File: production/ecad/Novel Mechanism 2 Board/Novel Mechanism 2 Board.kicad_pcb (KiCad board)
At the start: 2 copper layers, 41.7 x 46.1 mm, 19 parts, among them J1 1755736, J2 1755736, J3 0532611271, U1 L9958SBTR, U2 TMCS1108A4BQDRQ1

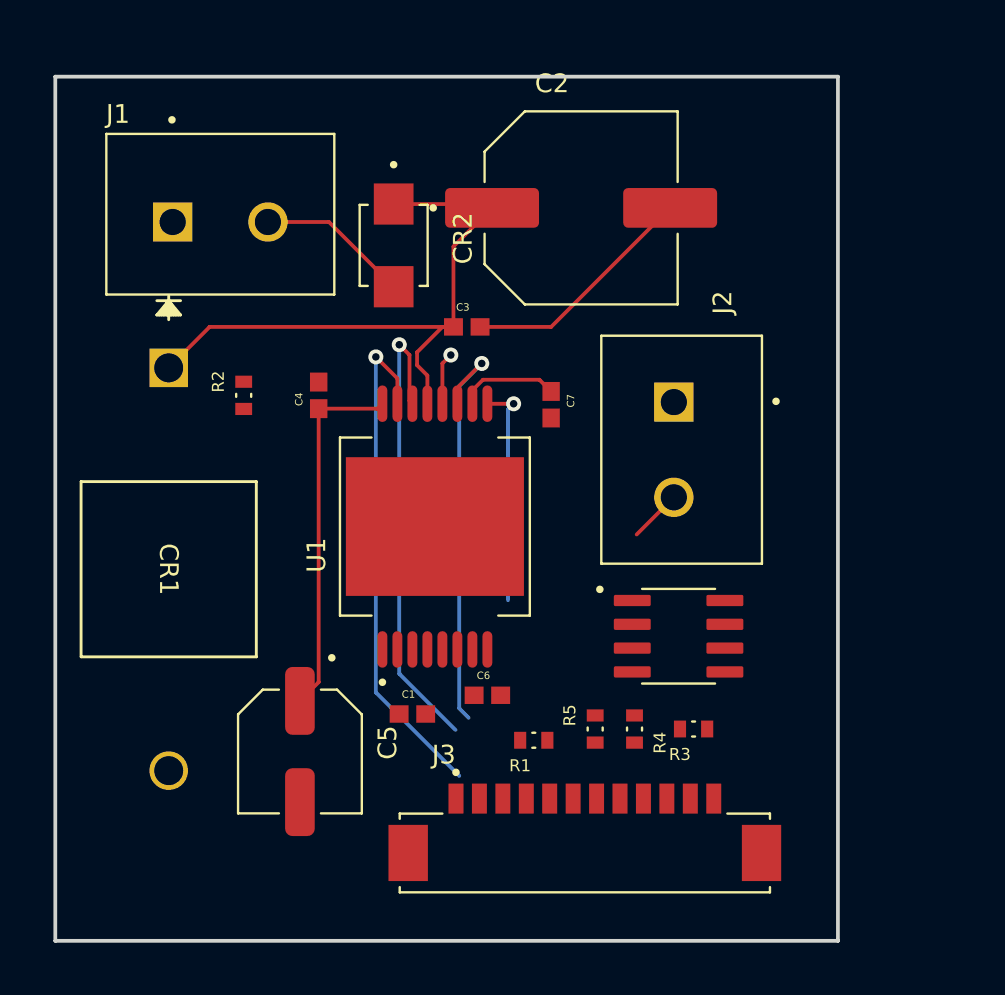
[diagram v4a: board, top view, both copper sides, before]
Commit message: updated design constraints
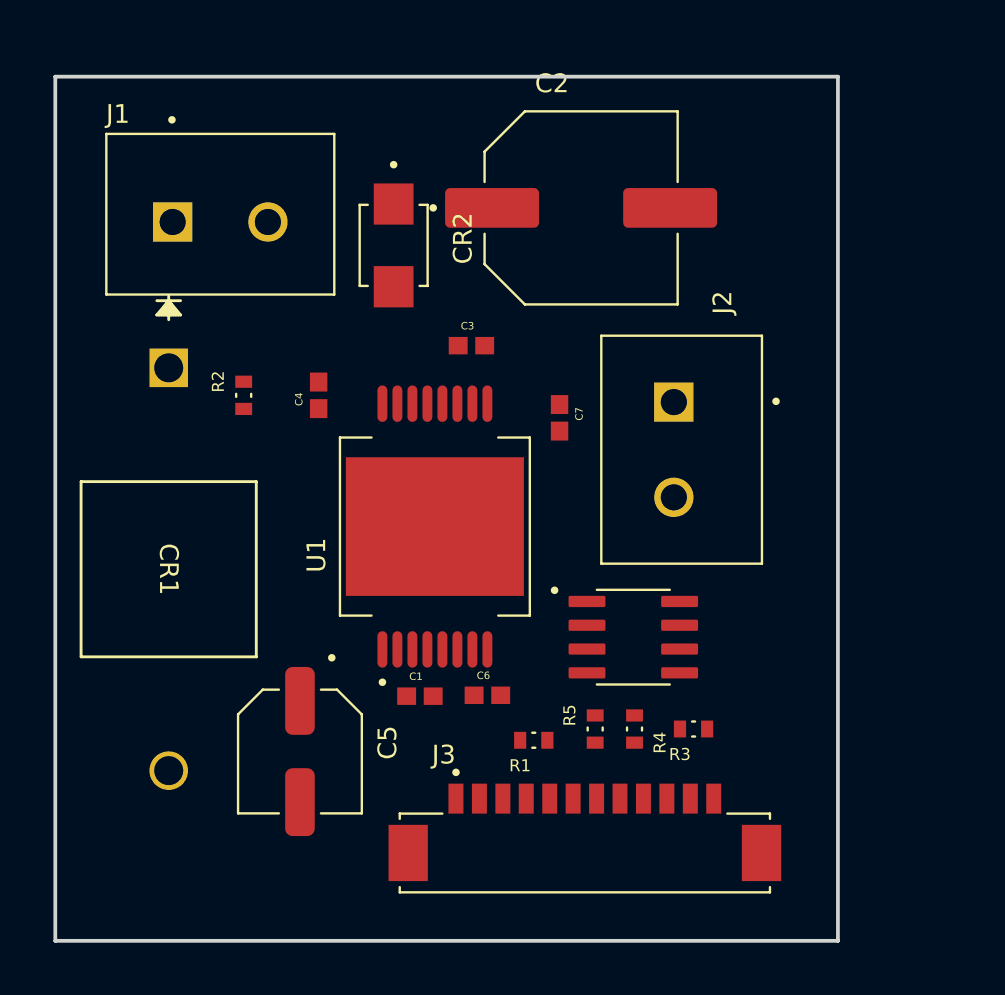
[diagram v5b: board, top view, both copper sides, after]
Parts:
- moved U2 2.42 mm to (147.8, 75.9)
- moved C1 1.03 mm to (136.4, 79.0)
- moved C3 1.03 mm to (139.2, 60.4)
- moved C7 0.83 mm to (143.8, 64.2)
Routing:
- net +15V: track 34.1 -> 0.00 mm
- net /SCK: track 27.2 -> 0.00 mm, vias 1 -> 0
- net /SI: track 25.2 -> 0.00 mm, vias 1 -> 0
- net /PWM: track 22.3 -> 0.00 mm, vias 1 -> 0
- net +5V: track 19.7 -> 0.00 mm
- net GND: track 12.8 -> 0.00 mm
- net /Enable: track 12.7 -> 0.00 mm, vias 1 -> 0
- net Net-(CR2-Pad2): track 8.14 -> 0.00 mm
- net Net-(U1-OUT2): track 5.40 -> 0.00 mm
- net Net-(U2-IN-): track 2.80 -> 0.00 mm
- net Net-(U1-REXT): track 2.78 -> 0.00 mm, vias 1 -> 0
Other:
- copper layers 2 -> 4
- rule pad_to_mask_clearance: 0.05 -> 0
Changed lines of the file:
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@@
   (layers
     (0 "F.Cu" signal)
+    (1 "In1.Cu" power)
+    (2 "In2.Cu" power)
     (31 "B.Cu" signal)
     (32 "B.Adhes" user "B.Adhesive")
@@
       (layer "F.Mask" (type "Top Solder Mask") (thickness 0.01))
       (layer "F.Cu" (type "copper") (thickness 0.035))
-      (layer "dielectric 1" (type "core") (thickness 1.51) (material "FR4") (epsilon_r 4.5) (loss_tangent 0.02))
+      (layer "dielectric 1" (type "prepreg") (thickness 0.1) (material "FR4") (epsilon_r 4.5) (loss_tangent 0.02))
+      (layer "In1.Cu" (type "copper") (thickness 0.035))
+      (layer "dielectric 2" (type "core") (thickness 1.24) (material "FR4") (epsilon_r 4.5) (loss_tangent 0.02))
+      (layer "In2.Cu" (type "copper") (thickness 0.035))
+      (layer "dielectric 3" (type "prepreg") (thickness 0.1) (material "FR4") (epsilon_r 4.5) (loss_tangent 0.02))
       (layer "B.Cu" (type "copper") (thickness 0.035))
       (layer "B.Mask" (type "Bottom Solder Mask") (thickness 0.01))
@@
       (dielectric_constraints no)
     )
-    (pad_to_mask_clearance 0.05)
+    (pad_to_mask_clearance 0)
     (solder_mask_min_width 0.1)
     (pcbplotparams
@@
   )
   (footprint "Package_SO:TMCS1108A4BQDRQ1" (layer "F.Cu")
-    (at 150.2 75.85)
+    (at 147.785 75.9)
     (property "A1_MIN" "0.11")
     (property "A_MAX" "1.75")
@@
   )
   (footprint "Capacitor_SMD:CAP_0603" (layer "F.Cu")
-    (at 138.9 59.35)
+    (at 139.15 60.35)
     (property "Sheetfile" "Novel Mechanism 2 Board.kicad_sch")
     (property "Sheetname" "")
@@
   )
   (footprint "Capacitor_SMD:CAP_0603" (layer "F.Cu")
-    (at 143.4 63.5 -90)
+    (at 143.85 64.2 -90)
     (property "Sheetfile" "Novel Mechanism 2 Board.kicad_sch")
     (property "Sheetname" "")
@@
   )
   (footprint "Capacitor_SMD:CAP_0603" (layer "F.Cu")
-    (at 136 80)
+    (at 136.4 79.05)
     (property "Sheetfile" "Novel Mechanism 2 Board.kicad_sch")
     (property "Sheetname" "")
@@
   (gr_rect (start 116.95 46) (end 158.7 92.1)
     (stroke (width 0.2) (type default)) (fill none) (layer "Edge.Cuts"))
-  (segment (start 136.8 63.445) (end 136.8 61.942213) (width 0.2032) (layer "F.Cu") (net 1))
-  (segment (start 138.191 59.35) (end 138.191 55.059) (width 0.2032) (layer "F.Cu") (net 1))
-  (segment (start 138.191 55.059) (end 140.25 53) (width 0.2032) (layer "F.Cu") (net 1))
-  (segment (start 138.191 59.35) (end 125.18215 59.35) (width 0.2032) (layer "F.Cu") (net 1))
-  (segment (start 136.2484 61.390613) (end 136.2484 60.7016) (width 0.2032) (layer "F.Cu") (net 1))
-  (segment (start 137.6 59.35) (end 138.191 59.35) (width 0.2032) (layer "F.Cu") (net 1))
-  (segment (start 136.8 61.942213) (end 136.2484 61.390613) (width 0.2032) (layer "F.Cu") (net 1))
-  (segment (start 136.2484 60.7016) (end 137.6 59.35) (width 0.2032) (layer "F.Cu") (net 1))
-  (segment (start 125.18215 59.35) (end 123 61.53215) (width 0.2032) (layer "F.Cu") (net 1))
-  (segment (start 140.045 52.795) (end 140.25 53) (width 0.2032) (layer "F.Cu") (net 1))
-  (segment (start 135 52.795) (end 140.045 52.795) (width 0.2032) (layer "F.Cu") (net 1))
-  (segment (start 134.291 63.336) (end 134.4 63.445) (width 0.2032) (layer "F.Cu") (net 4))
-  (segment (start 134.136 63.709) (end 131 63.709) (width 0.2032) (layer "F.Cu") (net 4))
-  (segment (start 131 78.3) (end 130 79.3) (width 0.2032) (layer "F.Cu") (net 4))
-  (segment (start 131 63.709) (end 131 78.3) (width 0.2032) (layer "F.Cu") (net 4))
-  (segment (start 134.4 63.445) (end 134.136 63.709) (width 0.2032) (layer "F.Cu") (net 4))
-  (segment (start 143.4 59.35) (end 149.75 53) (width 0.2032) (layer "F.Cu") (net 5))
-  (segment (start 139.609 59.35) (end 143.4 59.35) (width 0.2032) (layer "F.Cu") (net 5))
-  (segment (start 142.7774 62.1684) (end 139.765307 62.1684) (width 0.2032) (layer "F.Cu") (net 7))
-  (segment (start 139.2 62.733707) (end 139.2 63.445) (width 0.2032) (layer "F.Cu") (net 7))
-  (segment (start 143.4 62.791) (end 142.7774 62.1684) (width 0.2032) (layer "F.Cu") (net 7))
-  (segment (start 139.765307 62.1684) (end 139.2 62.733707) (width 0.2032) (layer "F.Cu") (net 7))
-  (segment (start 128.2925 53.7525) (end 131.5475 53.7525) (width 0.2032) (layer "F.Cu") (net 8))
-  (segment (start 131.5475 53.7525) (end 135 57.205) (width 0.2032) (layer "F.Cu") (net 8))
-  (segment (start 140.005 63.45) (end 140 63.445) (width 0.2032) (layer "F.Cu") (net 9))
-  (segment (start 141.4 63.45) (end 140.005 63.45) (width 0.2032) (layer "F.Cu") (net 9))
-  (segment (start 140 63.445) (end 140 64.156293) (width 0.2032) (layer "F.Cu") (net 9))
-  (via (at 141.4 63.45) (size 0.8) (drill 0.4) (layers "F.Cu" "B.Cu") (net 9))
-  (segment (start 141.4 63.45) (end 141.1 63.75) (width 0.2032) (layer "B.Cu") (net 9))
-  (segment (start 141.1 63.75) (end 141.1 73.925) (width 0.2032) (layer "B.Cu") (net 9))
-  (segment (start 137.6 61.3) (end 137.6 63.445) (width 0.2032) (layer "F.Cu") (net 10))
-  (segment (start 138.05 60.85) (end 137.6 61.3) (width 0.2032) (layer "F.Cu") (net 10))
-  (via (at 138.05 60.85) (size 0.8) (drill 0.4) (layers "F.Cu" "B.Cu") (net 10))
-  (segment (start 139.7 61.3) (end 138.4 62.6) (width 0.2032) (layer "F.Cu") (net 15))
-  (segment (start 138.4 62.6) (end 138.4 63.445) (width 0.2032) (layer "F.Cu") (net 15))
-  (via (at 139.7 61.3) (size 0.8) (drill 0.4) (layers "F.Cu" "B.Cu") (net 15))
-  (segment (start 139.7 61.3) (end 138.5 62.5) (width 0.2032) (layer "B.Cu") (net 15))
-  (segment (start 138.5 62.5) (end 138.5 79.7) (width 0.2032) (layer "B.Cu") (net 15))
-  (segment (start 138.5 79.7) (end 139 80.2) (width 0.2032) (layer "B.Cu") (net 15))
-  (segment (start 135.8452 60.8452) (end 135.3 60.3) (width 0.2032) (layer "F.Cu") (net 16))
-  (segment (start 135.8452 63.2902) (end 135.8452 60.8452) (width 0.2032) (layer "F.Cu") (net 16))
-  (segment (start 136 63.445) (end 135.8452 63.2902) (width 0.2032) (layer "F.Cu") (net 16))
-  (via (at 135.3 60.3) (size 0.8) (drill 0.4) (layers "F.Cu" "B.Cu") (net 16))
-  (segment (start 135.3 77.85) (end 138.3 80.85) (width 0.2032) (layer "B.Cu") (net 16))
-  (segment (start 135.3 60.3) (end 135.3 77.85) (width 0.2032) (layer "B.Cu") (net 16))
-  (segment (start 135.2 63.445) (end 135.2 62.1) (width 0.2032) (layer "F.Cu") (net 17))
-  (segment (start 135.2 62.1) (end 134.05 60.95) (width 0.2032) (layer "F.Cu") (net 17))
-  (via (at 134.05 60.95) (size 0.8) (drill 0.4) (layers "F.Cu" "B.Cu") (net 17))
-  (segment (start 134.05 78.85) (end 138.5 83.3) (width 0.2032) (layer "B.Cu") (net 17))
-  (segment (start 134.05 60.95) (end 134.05 78.85) (width 0.2032) (layer "B.Cu") (net 17))
-  (segment (start 149.9475 68.44) (end 147.965 70.4225) (width 0.2032) (layer "F.Cu") (net 18))
 )

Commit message: signal routing complete!
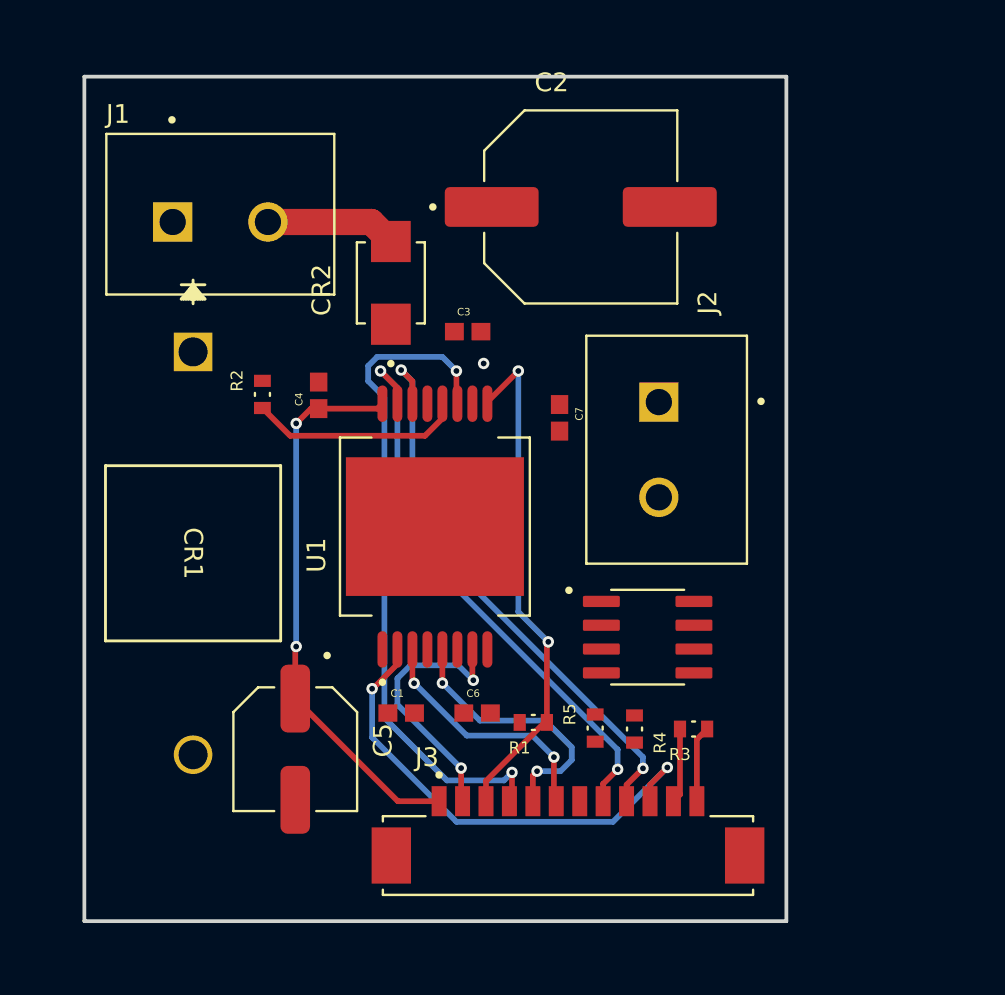
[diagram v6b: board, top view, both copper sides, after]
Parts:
- moved CR2 2.01 mm to (134.8, 57.0), turned to 90 degrees
- moved CR1 1.55 mm to (124.3, 60.7)
- moved C1 1.35 mm to (135.4, 80.0)
- moved C6 1.10 mm to (139.4, 80.0)
- moved R2 1.00 mm to (128.0, 63.0)
- moved R1 0.95 mm to (142.4, 80.5)
- moved J3 0.91 mm to (144.3, 87.5)
- moved J2 0.80 mm to (145.3, 59.8)
- moved C3 0.78 mm to (138.9, 59.6)
- moved U2 0.77 mm to (148.6, 75.9)
- moved C5 0.28 mm to (129.8, 81.9)
- moved C2 0.05 mm to (145.0, 53.0)
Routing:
- net /PWM: track 0.00 -> 36.1 mm, vias 0 -> 2
- net /SI: track 0.00 -> 30.7 mm, vias 0 -> 2
- net /SCK: track 0.00 -> 30.6 mm, vias 0 -> 2
- net +5V: track 0.00 -> 29.7 mm, vias 0 -> 2
- net /Enable: track 0.00 -> 27.5 mm, vias 0 -> 2
- net /SO: track 0.00 -> 26.3 mm, vias 0 -> 2
- net /Direction: track 0.00 -> 14.6 mm, vias 0 -> 2
- net /Disable: track 0.00 -> 14.3 mm, vias 0 -> 2
- net /ChipSel: track 0.00 -> 13.3 mm, vias 0 -> 2
- net Net-(U1-REXT): track 0.00 -> 12.2 mm
- net Net-(CR2-Pad2): track 0.00 -> 6.99 mm
- net Net-(J3-Pad12): track 0.00 -> 4.08 mm
- net /DET: track 0.00 -> 4.02 mm
- net Net-(U1-OUT2): vias 0 -> 1
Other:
- board size 41.7 x 46.1 mm -> 37.4 x 45 mm
- copper layers 4 -> 2

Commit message: preliminary copper zones
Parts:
- moved C3 7.95 mm to (131.0, 59.5), turned to 180 degrees
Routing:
- net +15V: track 0.00 -> 5.05 mm
- net Net-(U1-OUT2): vias 1 -> 0
- added copper zone on F.Cu, net +15V
- added copper zone on F.Cu, net Net-(U1-OUT2)
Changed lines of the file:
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@@
   )
   (footprint "Capacitor_SMD:CAP_0603" (layer "F.Cu")
-    (at 138.95 59.6)
+    (at 131 59.5 180)
     (property "Sheetfile" "Novel Mechanism 2 Board.kicad_sch")
     (property "Sheetname" "")
@@
     (fp_line (start 0.85 0.45) (end 0.85 -0.45)
       (stroke (width 0.127) (type solid)) (layer "F.Fab"))
-    (pad "1" smd rect (at -0.709 0) (size 1.01 0.93) (layers "F.Cu" "F.Paste" "F.Mask")
+    (pad "1" smd rect (at -0.709 0 180) (size 1.01 0.93) (layers "F.Cu" "F.Paste" "F.Mask")
       (net 1 "+15V") (pintype "passive") (solder_mask_margin 0.102))
-    (pad "2" smd rect (at 0.709 0) (size 1.01 0.93) (layers "F.Cu" "F.Paste" "F.Mask")
+    (pad "2" smd rect (at 0.709 0 180) (size 1.01 0.93) (layers "F.Cu" "F.Paste" "F.Mask")
       (net 5 "GND") (pintype "passive") (solder_mask_margin 0.102))
   )
@@
   (gr_rect (start 118.5 46) (end 155.95 91.05)
     (stroke (width 0.2) (type default)) (fill none) (layer "Edge.Cuts"))
+  (segment (start 136.8 61.155) (end 134.85 59.205) (width 0.508) (layer "F.Cu") (net 1))
+  (segment (start 136.8 63.445) (end 136.8 61.155) (width 0.508) (layer "F.Cu") (net 1))
   (segment (start 151.175 84.65) (end 151.175 81.35) (width 0.3048) (layer "F.Cu") (net 3))
   (segment (start 151.175 81.35) (end 151.725 80.8) (width 0.3048) (layer "F.Cu") (net 3))
@@
   (via (at 129.8 64.5) (size 0.6096) (drill 0.3048) (layers "F.Cu" "B.Cu") (net 4))
   (segment (start 129.8 64.5) (end 129.8 76.4) (width 0.3048) (layer "B.Cu") (net 4))
-  (via (at 139.8 61.3) (size 0.6096) (drill 0.3048) (layers "F.Cu" "B.Cu") (net 7))
   (segment (start 128.2925 53.7525) (end 133.8075 53.7525) (width 1.4) (layer "F.Cu") (net 8))
   (segment (start 133.8075 53.7525) (end 134.85 54.795) (width 1.4) (layer "F.Cu") (net 8))
@@
   (segment (start 149.925 84.65) (end 149.9 84.65) (width 0.3048) (layer "F.Cu") (net 21))
   (segment (start 149.925 84.65) (end 150.275 84.3) (width 0.3048) (layer "F.Cu") (net 21))
+  (zone (net 7) (net_name "Net-(U1-OUT2)") (layer "F.Cu") (hatch edge 0.5)
+    (priority 1)
+    (connect_pads (clearance 0.5))
+    (min_thickness 0.25) (filled_areas_thickness no)
+    (fill (thermal_gap 0.5) (thermal_bridge_width 0.5))
+    (polygon
+      (pts
+        (xy 140 65)
+        (xy 156.5 65)
+        (xy 156.5 61)
+        (xy 140 61)
+      )
+    )
+  )
+  (zone (net 1) (net_name "+15V") (layer "F.Cu") (hatch edge 0.5)
+    (connect_pads (clearance 0.5))
+    (min_thickness 0.25) (filled_areas_thickness no)
+    (fill (thermal_gap 0.5) (thermal_bridge_width 0.5))
+    (polygon
+      (pts
+        (xy 118 45)
+        (xy 144.5 45)
+        (xy 144.5 57)
+        (xy 137 57)
+        (xy 137 61)
+        (xy 126.5 61)
+        (xy 126.5 64)
+        (xy 118 64)
+      )
+    )
+  )
 )
